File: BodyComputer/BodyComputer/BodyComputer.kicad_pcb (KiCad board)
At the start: 2 copper layers, 151.5 x 130 mm, 356 parts, among them J1 Screw_Terminal_01x02, J10 Conn_02x03_Odd_Even, J11 SS-6488-FLS, J12 USB_B_Mini, J13 Conn_02x05_Odd_Even, J14 Conn_02x05_Odd_Even, J15 Screw_Terminal_01x02, J16 Screw_Terminal_01x02, J17 Screw_Terminal_01x02, J18 Screw_Terminal_01x02, J19 Screw_Terminal_01x02, J2 Screw_Terminal_01x02, J20 Screw_Terminal_01x02, J21 Screw_Terminal_01x02, J22 Screw_Terminal_01x03, J23 Screw_Terminal_01x02, J24 Screw_Terminal_01x02, J25 Screw_Terminal_01x03, J26 Screw_Terminal_01x02, J27 Screw_Terminal_01x02, J28 Screw_Terminal_01x02, J29 Screw_Terminal_01x02, J3 Screw_Terminal_01x03, J30 Screw_Terminal_01x02, J31 Screw_Terminal_01x02, J32 Screw_Terminal_01x03, J33 Screw_Terminal_01x02, J34 Screw_Terminal_01x02, J35 Conn_01x02, J36 Conn_01x08, J37 Conn_01x02, J38 Conn_01x03, J39 Conn_01x02, J4 Screw_Terminal_01x03, J5 Screw_Terminal_01x03, J6 Screw_Terminal_01x03, J7 MicroSD, J8 SS-6488-FLS, J9 Conn_02x05_Odd_Even, Q1 Q_NPN_BCE, Q10 IRLML2060, Q11 IRLML2060, Q12 IRLML2060, Q13 IRLML2060, Q14 IRLML2060, Q15 IRLML2060, Q16 IRLML2060, Q17 IRLML2060, Q18 IRLML2060, Q2 IRLML2060, Q3 IRLML2060, Q4 IRLML2060, Q5 IRLML2060, Q6 IRLML2060, Q7 IRLML2060, Q8 IRLML2060, Q9 IRLML2060, SW1 SW_Push, U1 ADP2302ARDZ-3.3, U2 AZ1117-5.0, U3 EEPROM, U4 EEPROM, U5 NodeMCU_1.0_(ESP-12E), U6 LM358, U7 STM32F103VETx, Y1 8-16MHz

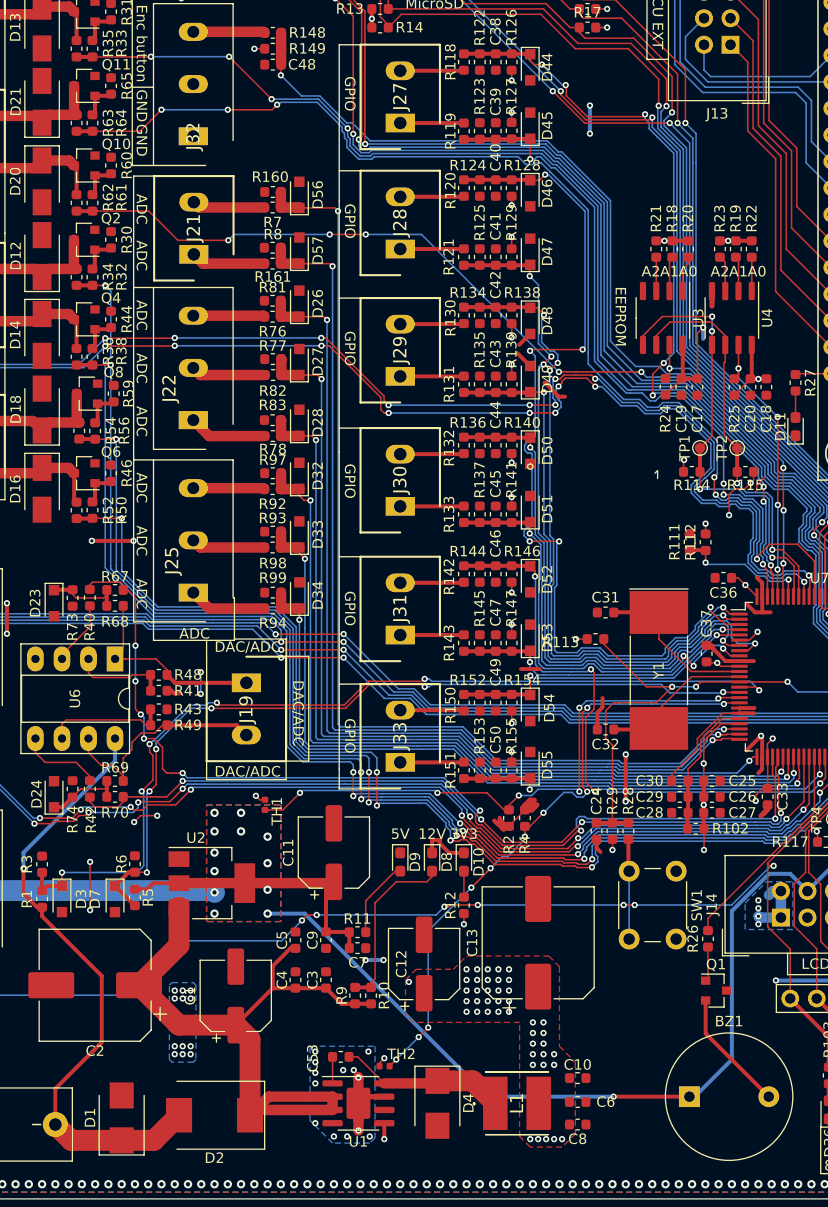
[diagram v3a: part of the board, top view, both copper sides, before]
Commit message: Body Computer [DONE]
Body Computer done as a 2-layer board and put into prototype production, schematics and PCBs created.
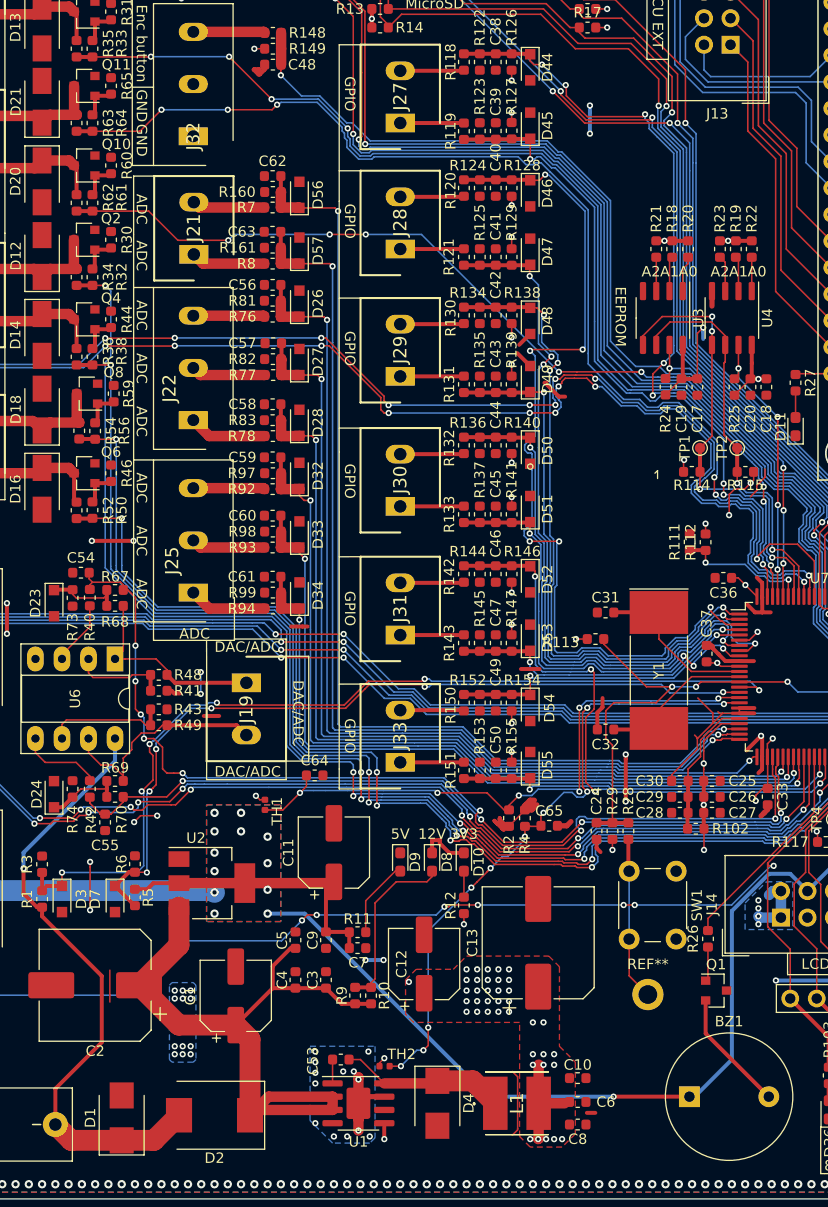
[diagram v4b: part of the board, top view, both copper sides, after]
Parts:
- added C54: 100n, Capacitor_SMD:C_0603_1608Metric, F.Cu at (58.4, 89.2)
- added C55: 100n, Capacitor_SMD:C_0603_1608Metric, F.Cu at (60.7, 113.1)
- added C56: 100n, Capacitor_SMD:C_0603_1608Metric, F.Cu at (76.7, 61.6)
- added C57: 100n, Capacitor_SMD:C_0603_1608Metric, F.Cu at (76.8, 67.2)
- added C58: 100n, Capacitor_SMD:C_0603_1608Metric, F.Cu at (76.7, 73.0)
- added C59: 100n, Capacitor_SMD:C_0603_1608Metric, F.Cu at (76.7, 78.1)
- added C60: 100n, Capacitor_SMD:C_0603_1608Metric, F.Cu at (76.7, 83.7)
- added C61: 100n, Capacitor_SMD:C_0603_1608Metric, F.Cu at (76.7, 89.5)
- added C62: 100n, Capacitor_SMD:C_0603_1608Metric, F.Cu at (76.7, 51.2)
- added C63: 100n, Capacitor_SMD:C_0603_1608Metric, F.Cu at (76.7, 56.5)
- added C64: 100n, Capacitor_SMD:C_0603_1608Metric, F.Cu at (80.8, 108.6)
- added C65: 100n, Capacitor_SMD:C_0603_1608Metric, F.Cu at (103.2, 113.4)
- added REF**: MountingHole_2.2mm_M2_DIN965_Pad, MountingHole:MountingHole_2.2mm_M2_DIN965_Pad, F.Cu at (112.7, 129.5)
- moved C53 0.25 mm to (83.3, 135.8)
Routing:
- net GND: track 136.2 -> 161.2 mm
- net +3V3: track 131.7 -> 141.3 mm, vias 102 -> 98
- net Net-(R28-Pad1): track 9.58 -> 15.6 mm
- net /MCU/ADC_IN13: track 59.6 -> 61.7 mm
- net /MCU/ADC_IN12: track 56.9 -> 58.8 mm
- net (no net): track 12.2 -> 10.4 mm
- net /Inputs_Outputs/ADC_2: track 83.4 -> 84.9 mm
- net /Inputs_Outputs/ADC_6: track 68.1 -> 69.7 mm
- net /Inputs_Outputs/ADC_7: track 97.8 -> 99.3 mm
- net /Inputs_Outputs/ADC_5: track 72.8 -> 74.3 mm
- net /Inputs_Outputs/ADC_4: track 77.4 -> 78.9 mm
- net /Inputs_Outputs/ADC_8: track 92.8 -> 94.3 mm
- net /Inputs_Outputs/ADC_3: track 81.3 -> 82.8 mm
- net /Inputs_Outputs/ADC_1: track 87.8 -> 89.3 mm
- net /Inputs_Outputs/AN_IN2_DAC2_INPUT: track 78.0 -> 79.1 mm
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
